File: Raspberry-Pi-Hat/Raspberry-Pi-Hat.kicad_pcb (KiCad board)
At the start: 4 copper layers, 65 x 56 mm, 127 parts, among them J1 Screw_Terminal_01x04, J2 Screw_Terminal_01x02, J3 40HAT, J4 Screw_Terminal_01x02, J5 USB_B, J6 CONN_02X02, J7 USB_A, J8 USB_A, J9 CONN_01X02, Q1 DMG2305UX, Q2 DMMT5401, U1 ADM3490ExR, U2 CAT24C32, U3 TCAN330, U4 LMZ13608, U5 TUSB4041I, U6 MCP2221AxSL, U7 MCP2221AxSL, U8 TPS2561, U9 TPS2561, Y1 24MHz

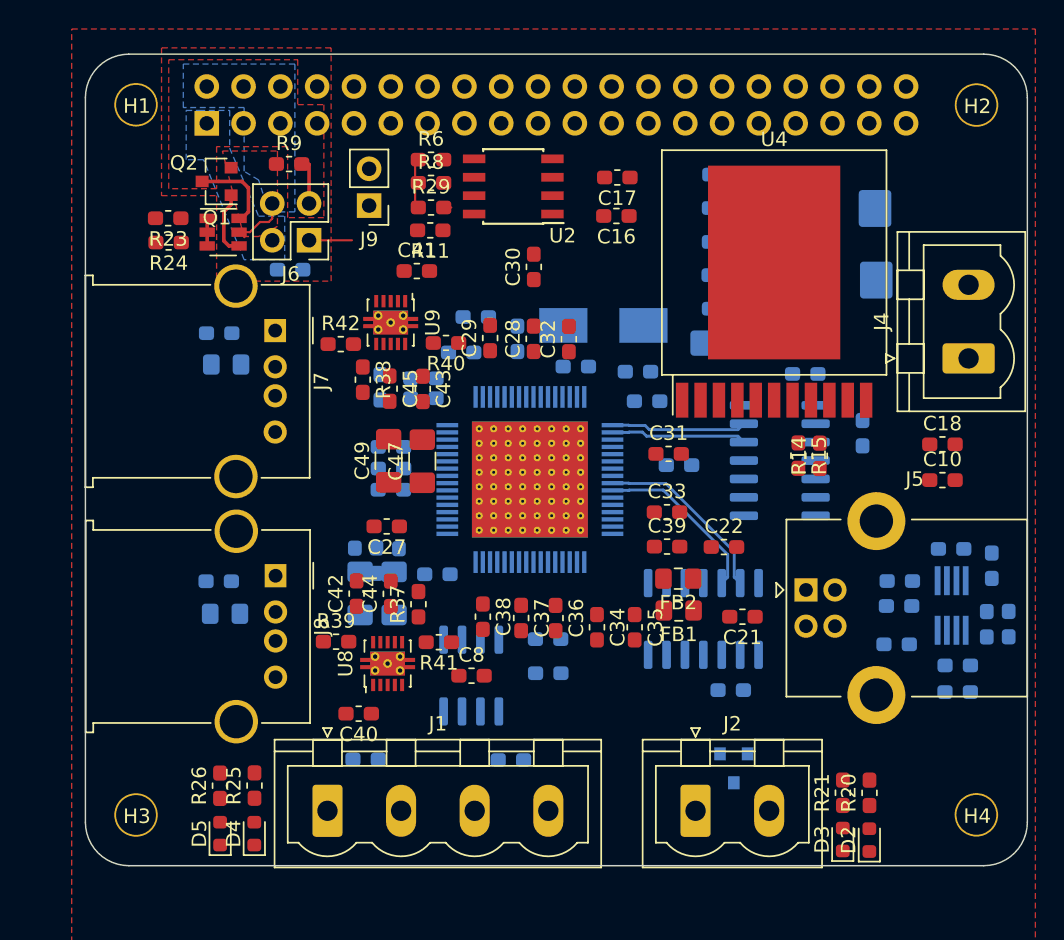
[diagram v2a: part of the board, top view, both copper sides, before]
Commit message: Routted diff pair
All USB lines is routed and most of the signal lines is routed as well.
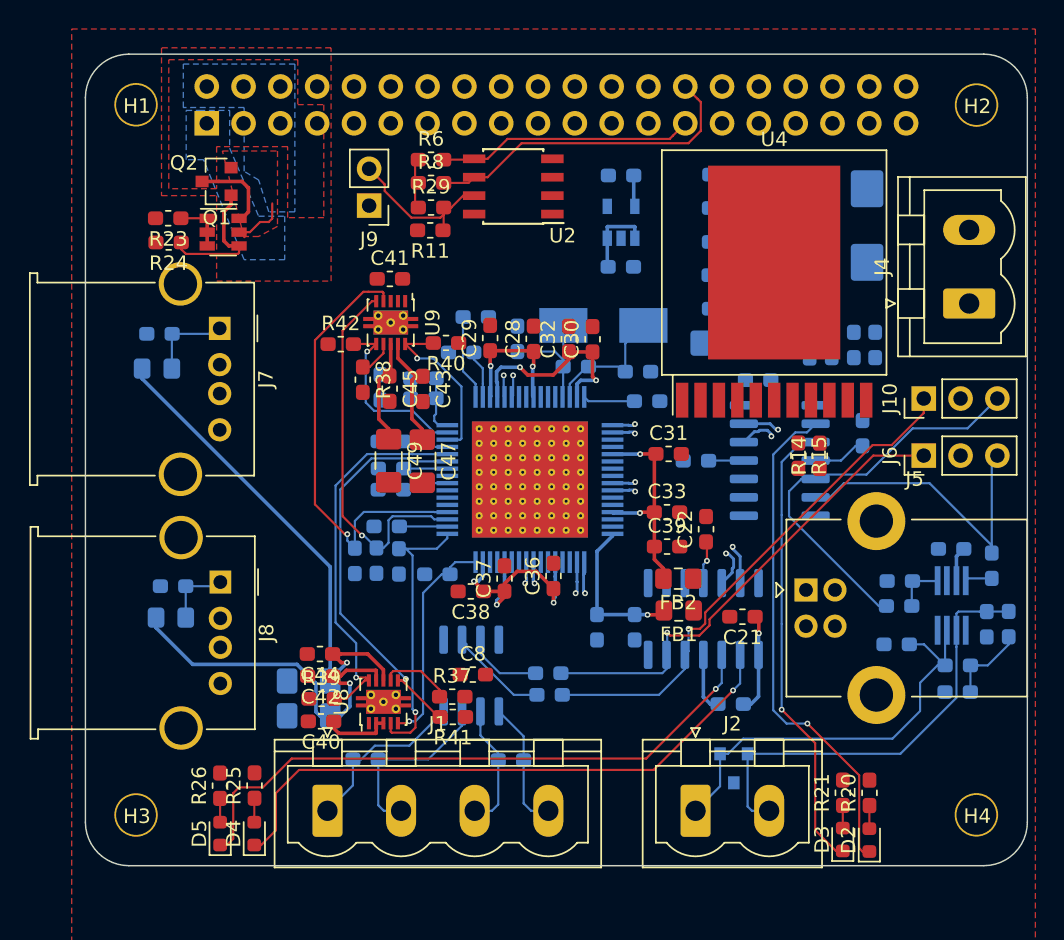
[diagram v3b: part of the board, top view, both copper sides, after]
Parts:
- removed R7, R9: DNP, Resistor_SMD:R_0603_1608Metric_Pad1.05x0.95mm_HandSolder
- added C54: 1uF, Capacitor_SMD:C_0603_1608Metric_Pad1.05x0.95mm_HandSolder, B.Cu at (115.5, 75.5)
- added C55: 1uF, Capacitor_SMD:C_0603_1608Metric_Pad1.05x0.95mm_HandSolder, B.Cu at (115.5, 69.2)
- added J10: Conn_01x03, Connector_PinHeader_2.54mm:PinHeader_1x03_P2.54mm_Vertical, F.Cu at (136.4, 84.6)
- added U11: TLV71211_SOT23-5, Package_TO_SOT_SMD:SOT-23-5, B.Cu at (115.5, 72.4)
- C10, C16, C17, C18, C27, C34, C35: moved to B.Cu
- J6: value CONN_02X02 -> Conn_01x03; footprint Connector_PinHeader_2.54mm:PinHeader_2x02_P2.54mm_Vertical -> Connector_PinHeader_2.54mm:PinHeader_1x03_P2.54mm_Vertical
- moved J6 44.9 mm to (136.4, 88.5), turned to 90 degrees
- moved C17 20.0 mm to (131.6, 80.9), turned to 90 degrees
- moved C16 20.0 mm to (133.0, 80.9), turned to 90 degrees
- moved C10 13.1 mm to (128.5, 80.9), turned to 90 degrees
- moved C18 10.3 mm to (130.0, 80.9), turned to 90 degrees
- moved C46 9.16 mm to (94.0, 106.5), turned to 180 degrees
- moved C48 8.45 mm to (94.0, 104.1), turned to 180 degrees
- moved R37 6.79 mm to (103.9, 105.2), turned to 0 degrees
- moved C30 6.43 mm to (113.5, 80.5)
- moved C44 6.41 mm to (94.7, 102.2), turned to 180 degrees
- moved C42 6.22 mm to (94.8, 103.7), turned to 180 degrees
- moved R41 5.25 mm to (103.9, 106.6)
- moved FB3 4.78 mm to (83.5, 82.5)
- moved C50 4.12 mm to (83.7, 80.1)
- moved R39 4.07 mm to (94.8, 105.3)
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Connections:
- J3 pad 1: /P3V3_HAT -> +3V3
- J3 pad 11: Net-(J3-Pad11) -> (no net)
- J3 pad 12: Net-(J3-Pad12) -> (no net)
- J3 pad 13: Net-(J3-Pad13) -> (no net)
- J3 pad 15: Net-(J3-Pad15) -> (no net)
- J3 pad 16: Net-(J3-Pad16) -> (no net)
- J3 pad 17: Net-(J3-Pad17) -> (no net)
- J3 pad 18: Net-(J3-Pad18) -> (no net)
- J3 pad 19: /SPI-MOSI-(GPIO10) -> (no net)
- J3 pad 2: /P5V_HAT -> /P5V
- J3 pad 21: /SPI-MISO-(GPIO9) -> (no net)
- J3 pad 22: Net-(J3-Pad22) -> (no net)
- J3 pad 23: /SPI-CLK-(GPIO11) -> (no net)
- J3 pad 24: Net-(J3-Pad24) -> (no net)
- J3 pad 26: Net-(J3-Pad26) -> (no net)
- J3 pad 29: Net-(J3-Pad29) -> (no net)
- J3 pad 3: /I2C-SDA-(GPIO2) -> (no net)
- J3 pad 31: Net-(J3-Pad31) -> (no net)
- J3 pad 32: Net-(J3-Pad32) -> (no net)
- J3 pad 33: Net-(J3-Pad33) -> (no net)
- J3 pad 35: Net-(J3-Pad35) -> (no net)
- J3 pad 36: Net-(J3-Pad36) -> (no net)
- J3 pad 37: Net-(J3-Pad37) -> (no net)
- J3 pad 38: Net-(J3-Pad38) -> (no net)
- J3 pad 4: /P5V_HAT -> /P5V
- J3 pad 40: Net-(J3-Pad40) -> (no net)
- J3 pad 5: /I2C-SCL-(GPIO3) -> (no net)
- J3 pad 7: Net-(J3-Pad7) -> (no net)
- J6 pad 1: +3V3 -> RX_NMEA183
- J6 pad 2: /P3V3_HAT -> /TXD(GPIO14)
- J6 pad 3: +5V -> RX_CAN
- Q1 pad 2: /P5V_HAT -> +5V
- Q1 pad 3: +5V -> /P5V
- Q2 pad 5: /P5V_HAT -> +5V
- Q2 pad 6: +5V -> /P5V
- U3 pad 5: Net-(U3-Pad5) -> (no net)
- U3 pad 8: Net-(U3-Pad8) -> (no net)
- U4 pad 4: Net-(U4-Pad4) -> (no net)
- U4 pad 9: Net-(U4-Pad9) -> (no net)
- U5 pad 23: Net-(U5-Pad23) -> (no net)
- U5 pad 24: Net-(U5-Pad24) -> (no net)
- U5 pad 26: Net-(U5-Pad26) -> (no net)
- U5 pad 27: Net-(U5-Pad27) -> (no net)
- U5 pad 28: Net-(U5-Pad28) -> (no net)
- U5 pad 35: Net-(U5-Pad35) -> (no net)
- U5 pad 36: Net-(U5-Pad36) -> (no net)
- U5 pad 38: Net-(U5-Pad38) -> (no net)
- U5 pad 39: Net-(U5-Pad39) -> (no net)
- U5 pad 40: Net-(U5-Pad40) -> (no net)
- U5 pad 43: Net-(U5-Pad43) -> (no net)
- U5 pad 44: Net-(U5-Pad44) -> (no net)
- U5 pad 46: Net-(U5-Pad46) -> (no net)
- U5 pad 47: Net-(U5-Pad47) -> (no net)
- U5 pad 5: Net-(U5-Pad5) -> (no net)
- U5 pad 51: Net-(U5-Pad51) -> (no net)
- U5 pad 52: Net-(U5-Pad52) -> (no net)
- U5 pad 54: Net-(U5-Pad54) -> (no net)
- U5 pad 55: Net-(U5-Pad55) -> (no net)
- U5 pad 58: Net-(U5-Pad58) -> (no net)
- U5 pad 59: Net-(U5-Pad59) -> (no net)
- U5 pad 6: Net-(U5-Pad6) -> (no net)
- U5 pad 61: Net-(U5-Pad61) -> (no net)
- U5 pad 62: Net-(U5-Pad62) -> (no net)
- U5 pad 7: Net-(U5-Pad7) -> (no net)
- U5 pad 9: Net-(U5-Pad9) -> (no net)
- U6 pad 10: Net-(U6-Pad10) -> (no net)
- U6 pad 7: Net-(U6-Pad7) -> (no net)
- U6 pad 8: Net-(U6-Pad8) -> (no net)
- U6 pad 9: Net-(U6-Pad9) -> (no net)
- U7 pad 10: Net-(U7-Pad10) -> (no net)
- U7 pad 7: Net-(U7-Pad7) -> (no net)
- U7 pad 8: Net-(U7-Pad8) -> (no net)
- U7 pad 9: Net-(U7-Pad9) -> (no net)
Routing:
- net /TXD(GPIO14): track 0.00 -> 58.9 mm
- net /RXD(GPIO15): track 0.00 -> 51.7 mm
- net /USB-hub/USB_UP_P: track 0.00 -> 44.2 mm, vias 0 -> 1
- net /USB-hub/USB_UP_N: track 0.00 -> 44.2 mm, vias 0 -> 1
- net Net-(D5-Pad1): track 0.00 -> 43.0 mm, vias 0 -> 1
- net Net-(D4-Pad1): track 0.00 -> 41.6 mm, vias 0 -> 1
- net Net-(C28-Pad1): track 0.00 -> 41.3 mm, vias 0 -> 7
- net /USB-hub/USB_4_P: track 0.00 -> 38.5 mm, vias 0 -> 1
- net /USB-hub/USB_4_N: track 0.00 -> 38.5 mm, vias 0 -> 1
- net TX_NMEA183: track 0.00 -> 35.9 mm, vias 0 -> 1
- net Net-(D2-Pad1): track 0.00 -> 35.1 mm, vias 0 -> 1
- net /USB-hub/DN4_VBUS: track 0.00 -> 34.6 mm, vias 0 -> 1
- net RX_NMEA183: track 0.00 -> 33.1 mm, vias 0 -> 1
- net Net-(D3-Pad1): track 0.00 -> 31.8 mm, vias 0 -> 1
- net PWRCTL1: track 0.00 -> 30.8 mm, vias 0 -> 1
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- added copper zone on B.Cu, net +3V3
- added copper zone on B.Cu, net /P5V
- added copper zone on F.Cu, net /P5V
- removed copper zone on B.Cu, net /P3V3_HAT
- removed copper zone on B.Cu, net /P5V_HAT
- removed copper zone on F.Cu, net /P5V_HAT

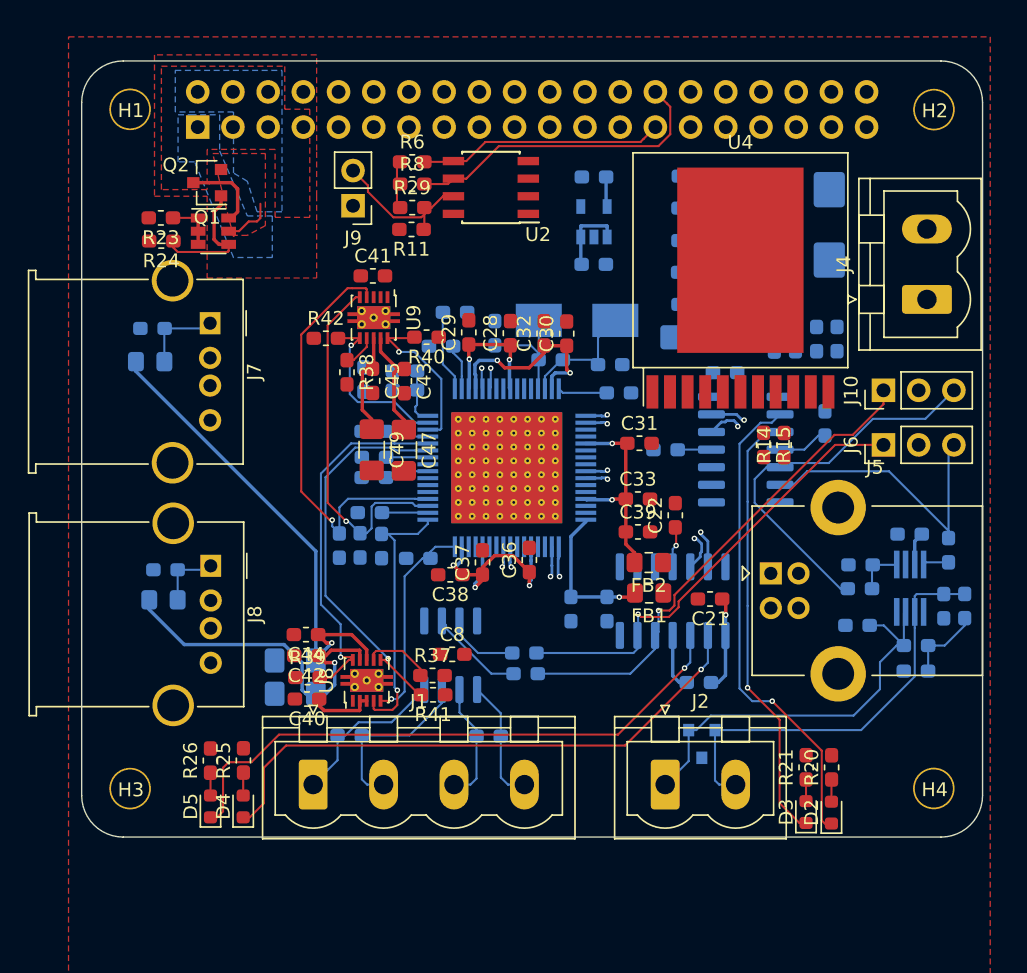
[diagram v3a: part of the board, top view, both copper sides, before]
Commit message: Change strategy
Remove USB hub, connect CAN to SPI and NMEA to RSPI serial.
Addition of RTC
Addition of Fan PWM connector
Plan to add a soft start button
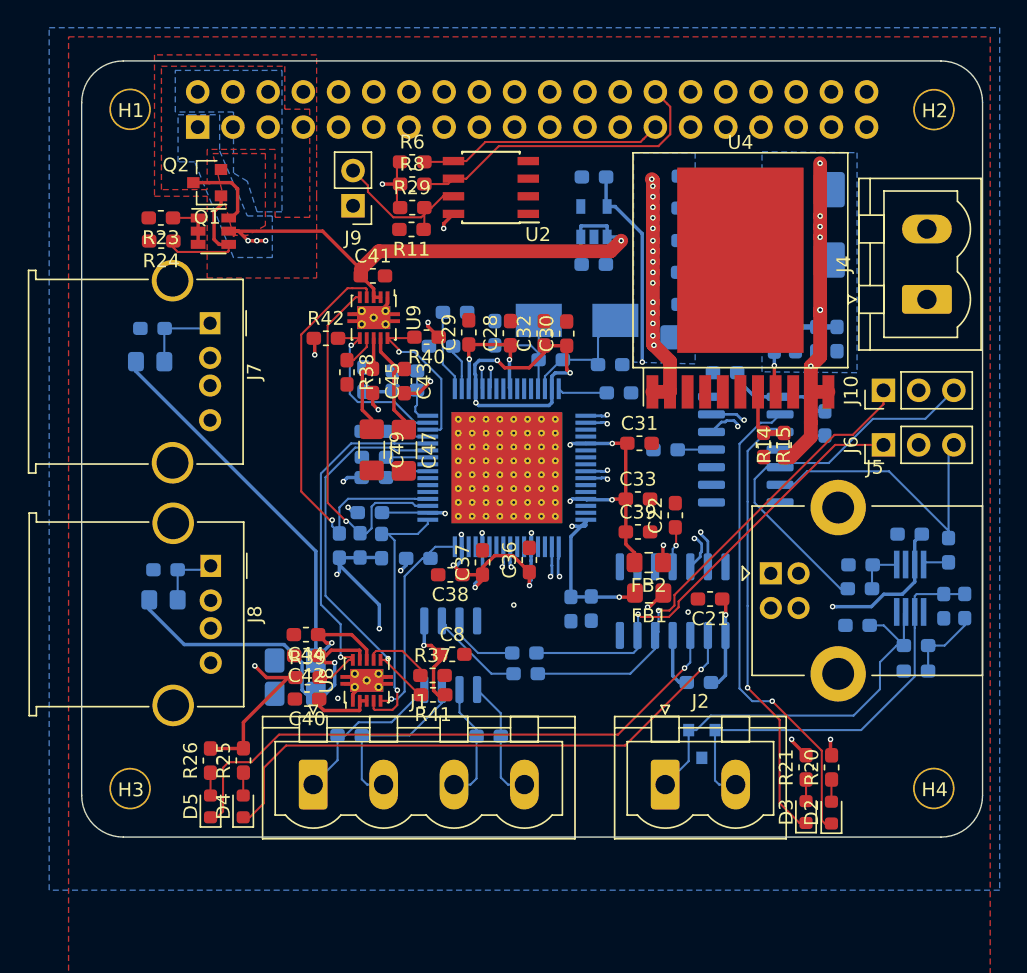
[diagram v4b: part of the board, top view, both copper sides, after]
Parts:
- moved C35 1.13 mm to (115.3, 100.3)
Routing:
- net +3V3: track 5.90 -> 185.3 mm, vias 0 -> 13
- net +5V: track 14.0 -> 103.5 mm, vias 0 -> 11
- net +12V: track 0.00 -> 48.8 mm, vias 0 -> 16
- net +1V1: track 2.16 -> 43.1 mm, vias 0 -> 2
- net Net-(C28-Pad1): track 41.3 -> 73.1 mm, vias 7 -> 12
- net Net-(C27-Pad1): track 28.2 -> 58.0 mm, vias 3 -> 6
- net GND: track 0.00 -> 24.0 mm, vias 0 -> 7
- net USB_1_VBUS: track 8.00 -> 15.8 mm
- net /RXD(GPIO15): track 51.7 -> 57.9 mm
- net Net-(R14-Pad2): track 0.00 -> 4.60 mm
- net Net-(C10-Pad1): track 0.00 -> 2.95 mm, vias 0 -> 1
- net /USB-hub/VBUS: track 0.00 -> 2.14 mm
- added copper zone on B.Cu, net +12V
- added copper zone on B.Cu, net +5V
- added copper zone on B.Cu, net GND
